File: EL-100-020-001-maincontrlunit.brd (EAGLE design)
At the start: 155.6 x 86 mm, 185 parts, among them T1 WS-TST-90°, U1 VNI4140K-32, U16 24AA256-I/SN, U19 ABS10-32.768KHZ-7-T, U2 VNI4140K-32, U3 VNI4140K-32, U8 MCP7940N-I/SN, U9 PMEG2005ET, X1 944-12-46-00, X10 S2L3.50/8/90G, X11 S2L3.50/8/90G, X12 S2L3.50/8/90G, X13 140-08-FLACHBAND1.27, X14 944-12-2-00, X2 944-12-46-00, X3 90G-14, X4 90G-14, X5 Q-063209, X6 Q-063209, X7 Q-063209, X8 Q-063209, X9 S2L3.50/8/90G

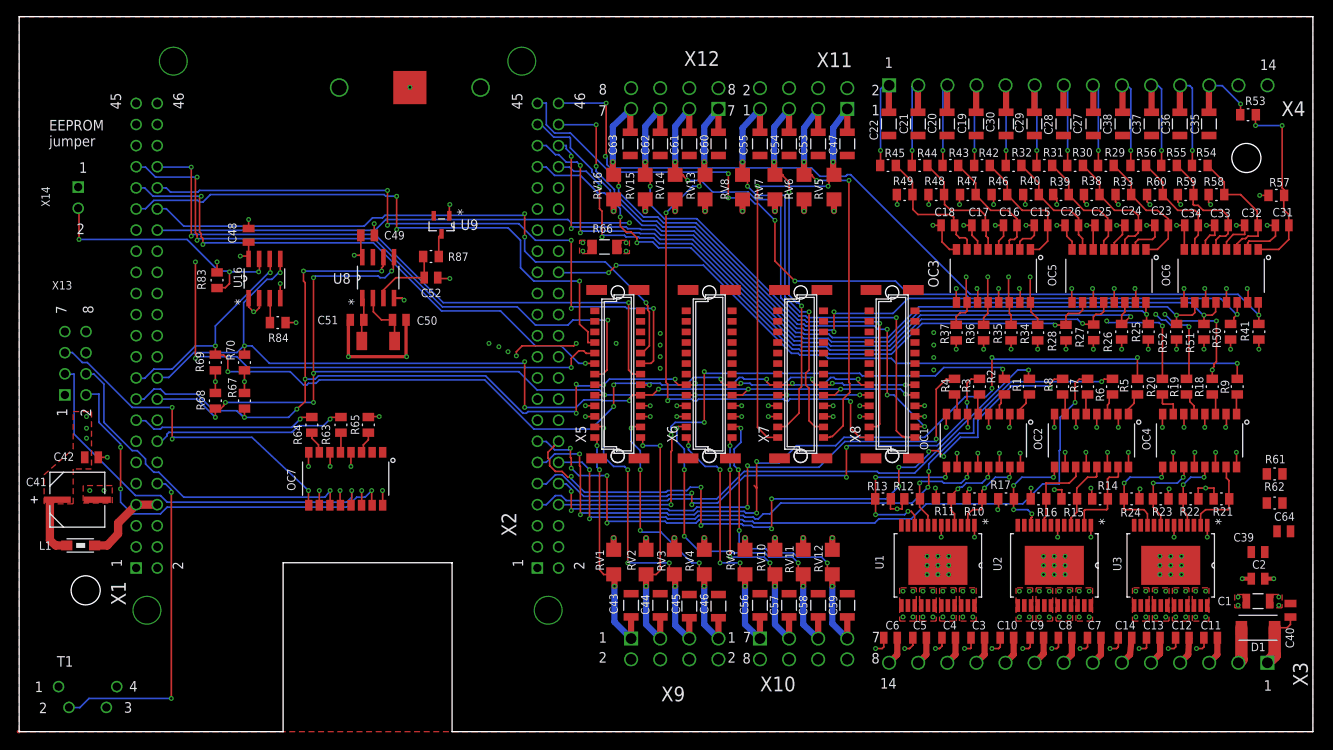
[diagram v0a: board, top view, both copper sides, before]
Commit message: update DIN rail
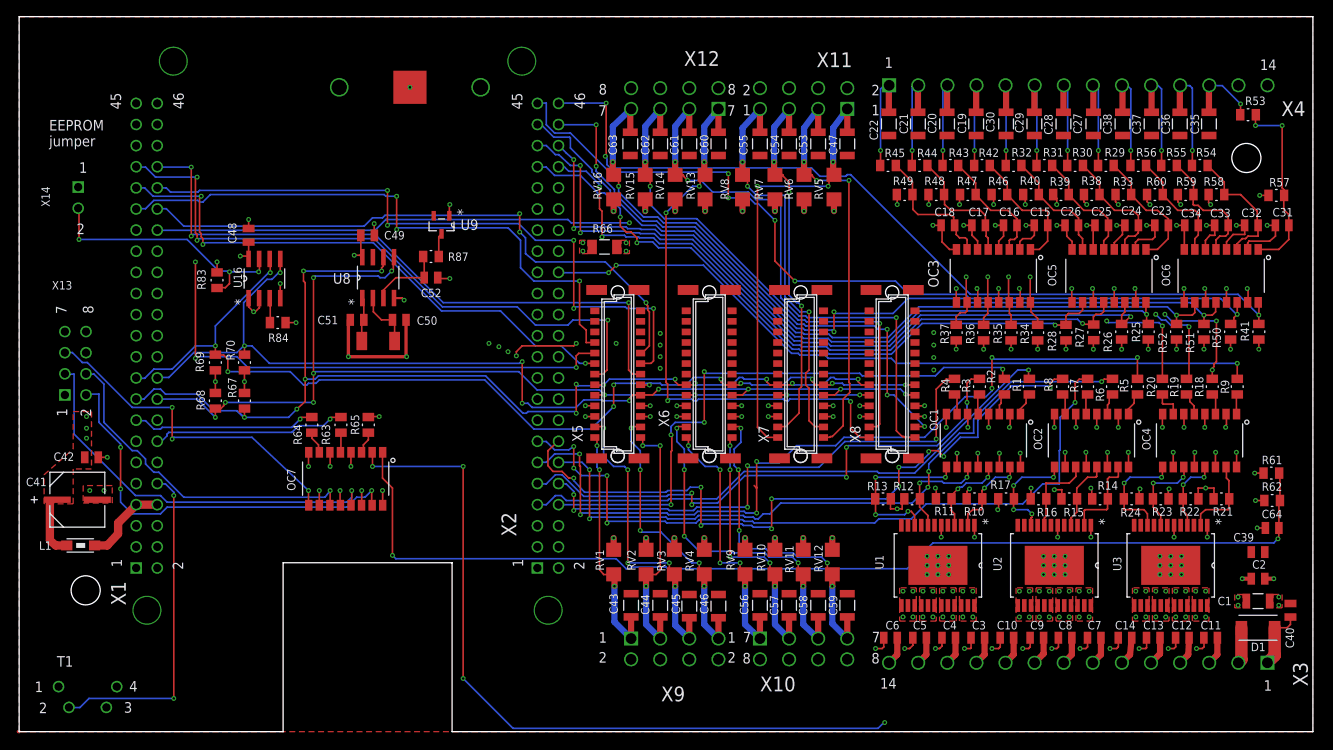
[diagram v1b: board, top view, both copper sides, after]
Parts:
- moved C64 1.46 mm to (150.7, 24.5), turned to 0 degrees
- moved R62 0.42 mm to (150.7, 27.8), turned to 180 degrees
- moved R61 0.41 mm to (150.6, 31.1), turned to 0 degrees
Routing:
- net N$40: track 0.00 -> 129.9 mm, vias 0 -> 2
- net 0V: track 132.2 -> 225.9 mm, vias 52 -> 58
- net +24V: track 31.0 -> 32.0 mm, vias 45 -> 46
- net P8_42: track 90.8 -> 90.1 mm

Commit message: Din rail
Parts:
- added U$1, U$2: (no value), marks:PASSER_SMD4
- moved C39 0.90 mm to (148.1, 21.6)
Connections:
- net VADC_1.8V: now also X5.B10
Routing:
- net VADC_1.8V: track 0.00 -> 80.7 mm, vias 0 -> 5
- net +24V: track 32.0 -> 33.1 mm, vias 46 -> 47
- net AIN1: track 78.2 -> 78.8 mm
- added copper zone on layer 1, net N$2
- added copper zone on layer 16, net PE
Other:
- board text added: "EL-100-020-001"
- board text added: "bottom"
- board text added: "rev. 1.0"
- board text added: "strasys"
- board text added: "top"

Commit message: extensions added
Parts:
- added C65: 1000pF, supply2:CAPC3216X88N
- C39, C40: value 4.7nF -> 4700pF
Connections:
- net AGND: now also C65.1
- net PE: now also C65.2
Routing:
- net AGND: vias 27 -> 29
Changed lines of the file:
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@@
 <layer number="17" name="Pads" color="2" fill="1" visible="yes" active="yes"/>
 <layer number="18" name="Vias" color="2" fill="1" visible="yes" active="yes"/>
-<layer number="19" name="Unrouted" color="6" fill="1" visible="yes" active="yes"/>
+<layer number="19" name="Unrouted" color="6" fill="1" visible="no" active="yes"/>
 <layer number="20" name="Dimension" color="15" fill="1" visible="yes" active="yes"/>
 <layer number="21" name="tPlace" color="7" fill="1" visible="yes" active="yes"/>
-<layer number="22" name="bPlace" color="7" fill="1" visible="yes" active="yes"/>
+<layer number="22" name="bPlace" color="7" fill="1" visible="no" active="yes"/>
 <layer number="23" name="tOrigins" color="15" fill="1" visible="yes" active="yes"/>
-<layer number="24" name="bOrigins" color="15" fill="1" visible="yes" active="yes"/>
+<layer number="24" name="bOrigins" color="15" fill="1" visible="no" active="yes"/>
 <layer number="25" name="tNames" color="7" fill="1" visible="yes" active="yes"/>
-<layer number="26" name="bNames" color="7" fill="1" visible="yes" active="yes"/>
+<layer number="26" name="bNames" color="7" fill="1" visible="no" active="yes"/>
 <layer number="27" name="tValues" color="7" fill="1" visible="no" active="yes"/>
 <layer number="28" name="bValues" color="7" fill="1" visible="no" active="yes"/>
@@
 <layer number="39" name="tKeepout" color="4" fill="11" visible="no" active="yes"/>
 <layer number="40" name="bKeepout" color="1" fill="11" visible="no" active="yes"/>
-<layer number="41" name="tRestrict" color="4" fill="10" visible="yes" active="yes"/>
+<layer number="41" name="tRestrict" color="4" fill="10" visible="no" active="yes"/>
 <layer number="42" name="bRestrict" color="1" fill="10" visible="no" active="yes"/>
 <layer number="43" name="vRestrict" color="2" fill="10" visible="no" active="yes"/>
-<layer number="44" name="Drills" color="7" fill="1" visible="no" active="yes"/>
+<layer number="44" name="Drills" color="7" fill="1" visible="yes" active="yes"/>
 <layer number="45" name="Holes" color="7" fill="1" visible="yes" active="yes"/>
 <layer number="46" name="Milling" color="3" fill="1" visible="yes" active="yes"/>
-<layer number="47" name="Measures" color="7" fill="1" visible="yes" active="yes"/>
-<layer number="48" name="Document" color="7" fill="1" visible="yes" active="yes"/>
-<layer number="49" name="Reference" color="7" fill="1" visible="yes" active="yes"/>
+<layer number="47" name="Measures" color="7" fill="1" visible="no" active="yes"/>
+<layer number="48" name="Document" color="7" fill="1" visible="no" active="yes"/>
+<layer number="49" name="Reference" color="7" fill="1" visible="no" active="yes"/>
 <layer number="50" name="dxf" color="7" fill="1" visible="no" active="no"/>
 <layer number="51" name="tDocu" color="7" fill="1" visible="yes" active="yes"/>
-<layer number="52" name="bDocu" color="7" fill="1" visible="yes" active="yes"/>
+<layer number="52" name="bDocu" color="7" fill="1" visible="no" active="yes"/>
 <layer number="53" name="tPadExt" color="7" fill="1" visible="no" active="no"/>
 <layer number="54" name="bPadExt" color="7" fill="1" visible="no" active="no"/>
@@
 <attribute name="OC_FARNELL" value="1514867" x="191.2" y="162" size="1.778" layer="27" rot="R180" display="off"/>
 <attribute name="WATTAGE" value="0.125 W" x="191.2" y="162" size="1.778" layer="27" rot="R180" display="off"/>
-<attribute name="NAME" x="105.1256" y="29.03" size="1.016" layer="25" font="vector" rot="SR0"/>
+<attribute name="NAME" x="107.67" y="29.0256" size="1.016" layer="25" font="vector" rot="SR90"/>
 <attribute name="VALUE" x="110.8544" y="31.175" size="2.0828" layer="27" ratio="10" rot="SR180"/>
 </element>
@@
 <attribute name="VALUE" x="136.98" y="57.34" size="1.27" layer="27" rot="R270"/>
 </element>
-<element name="C39" library="Kemet_By_element14_1" package="CAPC2013X88N" value="4.7nF" x="148.1" y="21.6" smashed="yes">
+<element name="C39" library="Kemet_By_element14_1" package="CAPC2013X88N" value="4700pF" x="148.1" y="21.6" smashed="yes">
 <attribute name="OC_NEWARK" value="32T6750" x="148.1" y="21.6" size="1.778" layer="27" display="off"/>
 <attribute name="TOLERANCE" value="±10%" x="148.1" y="21.6" size="1.778" layer="27" display="off"/>
@@
 <attribute name="VALUE" x="144.6456" y="18.425" size="2.0828" layer="27" ratio="10" rot="SR0"/>
 </element>
-<element name="C40" library="Kemet_By_element14_1" package="CAPC2013X88N" value="4.7nF" x="152.9" y="14.6" smashed="yes" rot="R270">
+<element name="C40" library="Kemet_By_element14_1" package="CAPC2013X88N" value="4700pF" x="152.9" y="14.6" smashed="yes" rot="R270">
 <attribute name="OC_NEWARK" value="32T6750" x="152.9" y="14.6" size="1.778" layer="27" rot="R270" display="off"/>
 <attribute name="TOLERANCE" value="±10%" x="152.9" y="14.6" size="1.778" layer="27" rot="R270" display="off"/>
@@
 <element name="U$1" library="marks" package="PASSER_SMD4" value="" x="5" y="82"/>
 <element name="U$2" library="marks" package="PASSER_SMD4" value="" x="151" y="4"/>
+<element name="C65" library="supply2" package="CAPC3216X88N" value="1000pF" x="68.3" y="81" smashed="yes" rot="R180">
+<attribute name="TOLERANCE" value="+/- 10%" x="68.3" y="81" size="1.778" layer="27" rot="R180" display="off"/>
+<attribute name="MPN" value="C1206C102KDRACTU" x="68.3" y="81" size="1.778" layer="27" rot="R180" display="off"/>
+<attribute name="SUPPLIER" value="Kemet" x="68.3" y="81" size="1.778" layer="27" rot="R180" display="off"/>
+<attribute name="VOLTAGE_RATING" value="1000V" x="68.3" y="81" size="1.778" layer="27" rot="R180" display="off"/>
+<attribute name="MF" value="KEMET" x="68.3" y="81" size="1.778" layer="27" rot="R180" display="off"/>
+<attribute name="OC_FARNELL" value="1826304" x="68.3" y="81" size="1.778" layer="27" rot="R180" display="off"/>
+<attribute name="NAME" x="67.0456" y="82.605" size="1.016" layer="25" font="vector" rot="SR0"/>
+<attribute name="VALUE" x="71.7544" y="84.937" size="2.0828" layer="27" ratio="10" rot="SR180"/>
+</element>
 </elements>
 <signals>
@@
 <contactref element="U8" pad="4"/>
 <contactref element="C49" pad="1"/>
-<polygon width="0.254" layer="2" thermals="no" rank="6">
+<polygon width="0.254" layer="2" isolate="0.2" thermals="no" rank="6">
 <vertex x="0" y="86"/>
 <vertex x="155.6" y="86"/>
@@
 <contactref element="X14" pad="P1"/>
 <contactref element="R66" pad="1"/>
-<polygon width="0.4064" layer="2" orphans="yes" thermals="no" rank="4">
+<polygon width="0.2" layer="2" isolate="0.2" orphans="yes" thermals="no" rank="4">
 <vertex x="109.9" y="54.5"/>
-<vertex x="150.1" y="54.4"/>
-<vertex x="150" y="54.4"/>
+<vertex x="150.1" y="54.7"/>
 <vertex x="150" y="35.6"/>
 <vertex x="109.9" y="35.6"/>
@@
 <vertex x="0" y="0"/>
 </polygon>
+<contactref element="C65" pad="2"/>
 </signal>
 <signal name="+3.3V">
@@
 <contactref element="X7" pad="B4"/>
 <contactref element="R66" pad="2"/>
-<polygon width="0.254" layer="2" isolate="0.254" orphans="yes" thermals="no" rank="3">
+<polygon width="0.254" layer="2" isolate="0.2" orphans="yes" thermals="no" rank="3">
 <vertex x="69.59" y="86.01"/>
 <vertex x="101.73" y="86.01"/>
-<vertex x="101.61" y="54.46"/>
+<vertex x="101.74" y="54.41"/>
 <vertex x="109.15" y="54.48"/>
 <vertex x="109.15" y="31.29"/>
-<vertex x="101.57" y="31.28"/>
-<vertex x="101.56" y="-0.01"/>
+<vertex x="101.67" y="31.28"/>
+<vertex x="102.06" y="-0.01"/>
 <vertex x="69.09" y="-0.01"/>
 <vertex x="69.1" y="42.7"/>
@@
 <wire x1="107.74" y1="37.92" x2="108.9" y2="37.92" width="0.2" layer="1"/>
 <wire x1="108.9" y1="37.92" x2="108.9" y2="37.9" width="0.2" layer="1"/>
+<contactref element="C65" pad="1"/>
+<via x="70.8" y="81.5" extent="1-16" drill="0.3"/>
+<via x="70.8" y="80.5" extent="1-16" drill="0.3"/>
+<polygon width="0.15" layer="1" orphans="yes" thermals="no">
+<vertex x="69.2" y="82.1"/>
+<vertex x="71.4" y="82.1"/>
+<vertex x="71.4" y="79.9"/>
+<vertex x="69.2" y="79.9"/>
+</polygon>
 </signal>
 <signal name="P8_19">
@@
 <contactref element="C40" pad="2"/>
 <contactref element="C1" pad="1"/>
-<polygon width="0.254" layer="2" orphans="yes" thermals="no" rank="2">
-<vertex x="102.1" y="86"/>
+<polygon width="0.254" layer="2" isolate="0.2" orphans="yes" thermals="no" rank="2">
+<vertex x="101.9" y="86"/>
 <vertex x="155.6" y="86"/>
 <vertex x="155.6" y="0"/>
-<vertex x="102.1" y="0"/>
-<vertex x="102.1" y="35.3"/>
+<vertex x="102" y="0"/>
+<vertex x="102" y="35.3"/>
 <vertex x="150.5" y="35.3"/>
-<vertex x="150.5" y="54.9"/>
-<vertex x="102.1" y="54.94"/>
+<vertex x="150.5" y="54.8"/>
+<vertex x="101.9" y="54.84"/>
 </polygon>
 <contactref element="D1" pad="1"/>

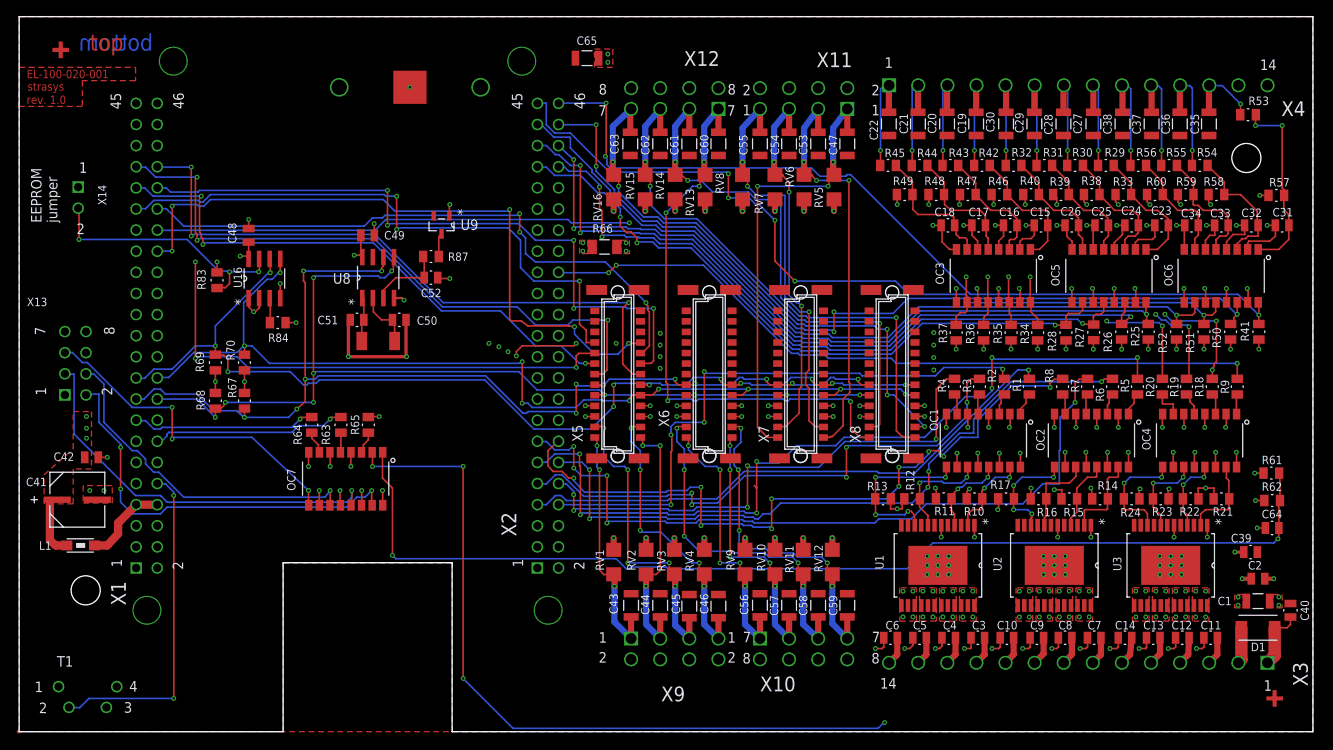
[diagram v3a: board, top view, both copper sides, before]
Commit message: DIN Rail extension
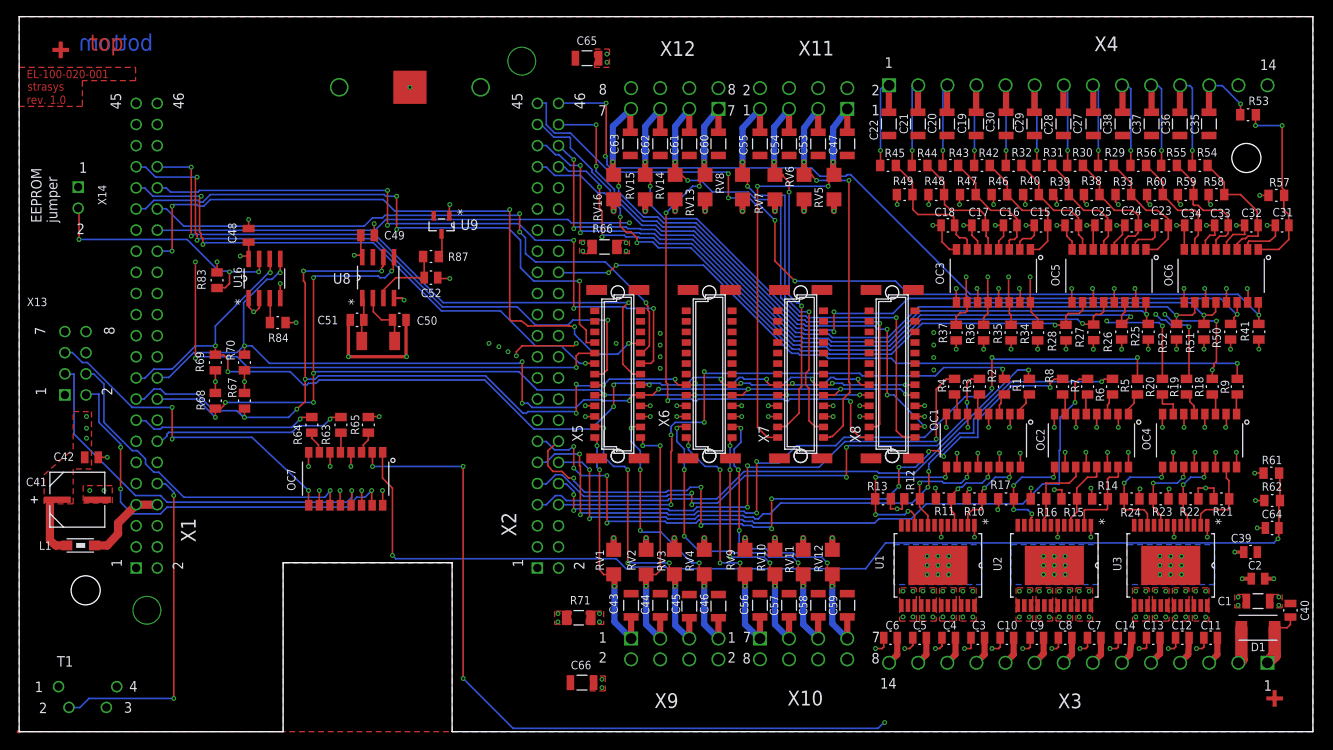
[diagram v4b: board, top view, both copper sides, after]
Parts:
- added C66: 1000pF, supply2:CAPC3216X88N
- added R71: 0 Ohms, Vishay_By_element14_Batch_1:RESC3216X71N
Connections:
- net AGND: now also C66.1, R71.2
- net DGND: now also R71.1
- net PE: now also C66.2
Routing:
- net N$46: track 2.85 -> 3.45 mm
- net DGND: vias 49 -> 51
- net AGND: vias 29 -> 33
- added copper zone on layer 16, net +24V

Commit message: prototype order status
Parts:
- moved C14 0.20 mm to (132.8, 11.3)
- moved C12 0.14 mm to (139.8, 11.4)
- moved C25 0.10 mm to (130.3, 60.9)
- moved C32 0.10 mm to (148.3, 60.9)
- moved C64 0.10 mm to (150.8, 24.5)
- moved R29 0.10 mm to (130.8, 68.1)
- moved R52 0.10 mm to (139.3, 48.1)
- moved R57 0.10 mm to (151.3, 64.5)
- moved R62 0.10 mm to (150.8, 27.8)
- moved C65 0.10 mm to (68.4, 81.0)
- moved R15 0.10 mm to (126.4, 28.0)
- moved R16 0.10 mm to (122.7, 28.0)
- moved R31 0.10 mm to (123.4, 68.1)
- moved R32 0.10 mm to (119.7, 68.1)
- moved R35 0.10 mm to (119.4, 48.0)
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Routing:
- net 0V: track 225.9 -> 228.4 mm
- net SYS5V_F: track 22.8 -> 23.4 mm
- net ANA_3.3: track 45.6 -> 46.1 mm
- net I2C1_SDA: track 119.3 -> 119.8 mm
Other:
- board size 155.6 x 86 mm -> 155.7 x 86 mm

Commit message: DIN-Rail-production
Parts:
- moved C45 0.30 mm to (80.6, 15.4)
- moved C46 0.30 mm to (84.1, 15.4)
- moved R61 0.20 mm to (150.9, 31.1)
- moved C43 0.20 mm to (73.6, 15.4)
- moved C44 0.20 mm to (77.1, 15.4)
- moved C56 0.20 mm to (89.1, 15.4)
- moved C57 0.20 mm to (92.6, 15.4)
- moved C58 0.20 mm to (96.1, 15.4)
- moved C59 0.20 mm to (99.6, 15.4)
- moved C25 0.10 mm to (130.2, 60.9)
- moved R52 0.10 mm to (139.2, 48.1)
- moved R39 0.10 mm to (125.3, 64.6)
- moved R47 0.10 mm to (114.1, 64.6)
- moved R48 0.10 mm to (110.3, 64.6)
- moved C15 0.10 mm to (122.9, 60.9)
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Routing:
- net 0V: track 228.4 -> 227.7 mm
- added copper zone on layer 15, net PE
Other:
- board size 155.7 x 86 mm -> 155.6 x 86 mm
- board text added: "EX 1"
- board text added: "EX 2"
- board text added: "EX 3"
- board text added: "EX 4"
